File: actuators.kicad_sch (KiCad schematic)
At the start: 3 parts, among them J12 PWM signals, row 1, J13 SERVO_5V pass-through, row 2, J14 GND, row 3

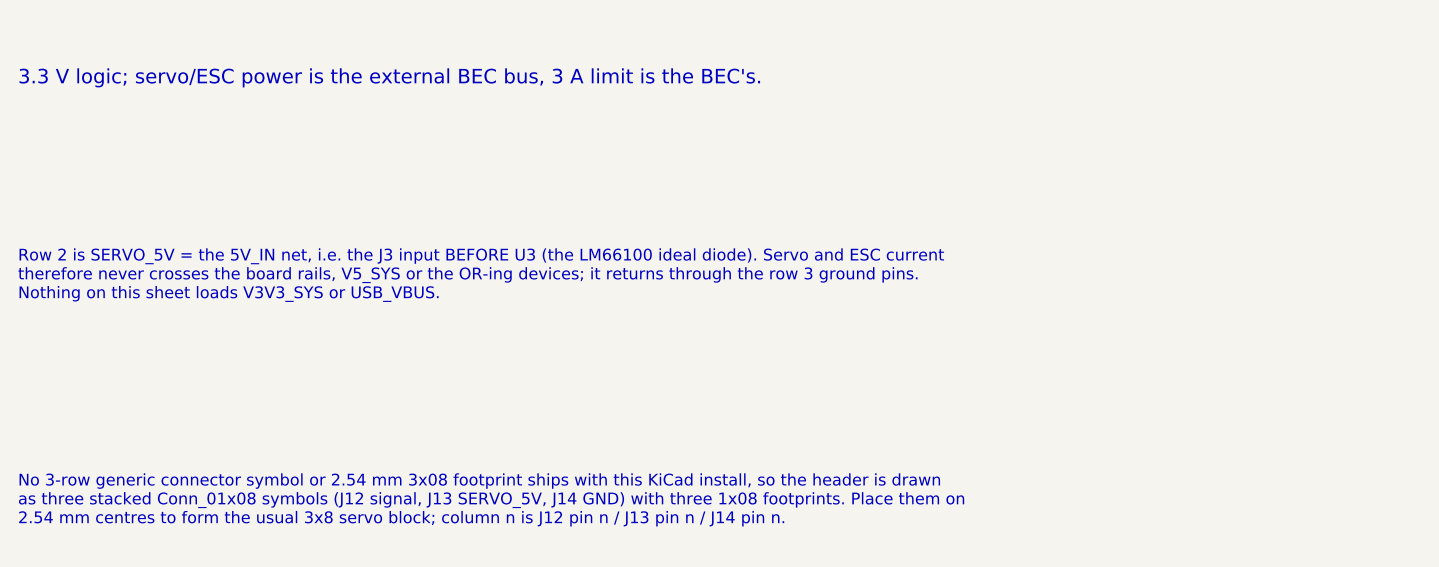
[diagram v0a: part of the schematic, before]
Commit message: Schematic review: TPS2121 input stage, DS-009 ports, sequencing and CS fixes; docs trimmed
Datasheet-grounded review of the full flight-controller schematic. Downstream
of the input everything verified pin-by-pin (TPS62913, TPS7A20, RP2354B,
BMI088/BMP581/ADXL375, W25Q128, microSD, PWM). The 5 V input stage did not:

- LM66100 (5.5 V rec-op / 6 V abs-max) replaced by one TPS2121 mux (U25):
  BEC priority on IN1, OV lockout ~5.86 V, current limit ~1.5 A, reverse
  blocking on both inputs, source status on GPIO39. Input spec 4.75-5.5 V.
- 5V_IN: 2x4.7 uF + 100 uF + SMAJ5.0A TVS; J3 JST-XH -> XT30PW-M (pin 1 GND).
- J6/J7/J9 reordered to Pixhawk DS-009 (VCC/sig/sig/GND); GPS/ELRS VCC 5 V.
- VIN_SENSE 22k/10k (full scale 10.6 V, was saturating at 5.5 V).
- TPS7A20 EN <- PWR_GOOD so V3V3_ANA rises after V3V3_SYS.
- RP2354B VREG_AVDD moved to V3V3_SYS (datasheet 6.1.8: must power up with
  VREG_VIN); ADC_AVDD stays on V3V3_ANA.
- 10k pull-ups on the four sensor chip-selects.
- ERC "global label appears once" re-enabled (0 hits).

Generator, netlist checker and SPICE decks updated (TPS2121 behavioral model,
new over-voltage and 2S mis-plug corners). Build idempotent, 143 pin mappings
PASS, ERC 0/0, all corners PASS.

Docs: POWER_*.md history removed, rationale folded into DESIGN_SPEC Decisions;
808 -> 290 lines across README, DESIGN_SPEC, LIBRARIES, simulations/README.

Co-Authored-By: Claude Fable 5.1 <noreply@anthropic.com>
Claude-Session: https://claude.ai/code/session_015cFNiWgf35VN2T43HaK8PE
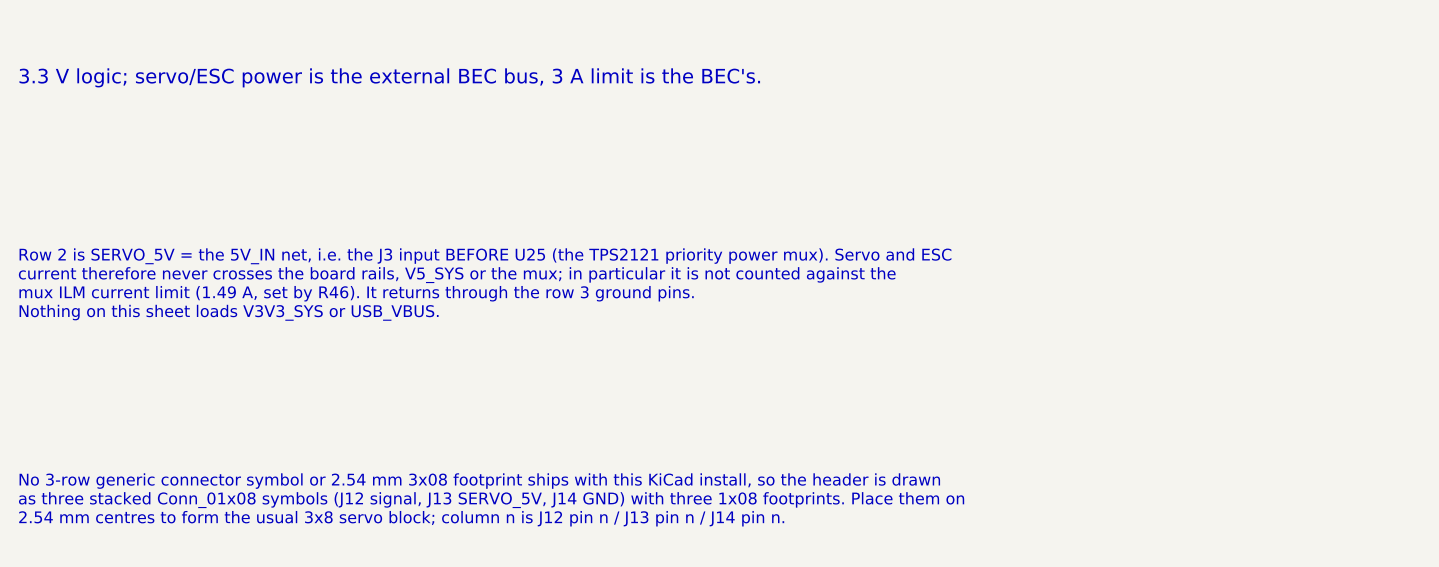
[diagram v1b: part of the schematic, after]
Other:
- note added: "Row 2 is SERVO_5V = the 5V_IN net, i.e. the J3 input BEFORE U25 (the TPS2121 priority power mux). Servo and ESC current therefore never crosses the board rails, V5_SYS or the mux; in particular it is not counted against the mux ILM current limit (1.49 A, set by R46). It returns through the row 3 ground pins. Nothing on this sheet loads V3V3_SYS or USB_VBUS."
- note removed: "Row 2 is SERVO_5V = the 5V_IN net, i.e. the J3 input BEFORE U3 (the LM66100 ideal diode). Servo and ESC current therefore never crosses the board rails, V5_SYS or the OR-ing devices; it returns through the row 3 ground pins. Nothing on this sheet loads V3V3_SYS or USB_VBUS."

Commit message: Physical design: VBAT-in buck, ESC pad row, pad-row IO, 50 mm single-sided board
Power: the FC now takes raw 2-6S VBAT from the MicoAir AM32 4-in-1 ESC pad
row (CURR TX M4 M3 M2 M1 VBAT GND, J3) through an AP63205WU 5 V/2 A buck
(U26, XGL4030-472, 3 x 22 uF) into the existing TPS2121 mux; XT30 and its
TVS removed. VBAT sense 100k/10k (36 V FS) on ADC0, ESC current sense on
ADC2, ESC KISS telemetry on GPIO30.

IO per the physical spec (DESIGN_SPEC "Physical design"): solder pad rows
for GPS/ELRS/MAG (JST-GH removed), DBG and buzzer; 3x4 servo block for
PWM5-8; 2x6 spare-IO block; WS2812C-2020 RGB LED replaces the two discrete
LEDs; buzzer moved off-board to pads; flash socket is the 150-mil SOIC-8
(W25Q64 default, APS6404L PSRAM alternative); four 4.0 mm grommet holes on
the 30.5 mm pattern. Passives moved to 0402/0603 for the single-sided
envelope.

Board: tools/setup_pcb.py regenerates MARV-V2.kicad_pcb from the netlist —
50 x 50 mm, 4-layer JLC 7628 stack-up, net classes incl. a 90 ohm USB pair,
edge-anchored connectors, coarse interior placement, silk pad labels.
DRC leaves only unrouted items. The BMP581 project footprint had its 2-pad
edges at +/-0.5 mm (corner pads overlapped, three nets shorted); corrected
to Bosch Fig. 32 (+/-0.25 mm, 0.20 mm gaps).

Checks: ERC 0/0, 217 pin mappings / 139 components, run_power_checks PASS,
audit 139/139, pcb DRC unrouted-only.

Co-Authored-By: Claude Fable 5.1 <noreply@anthropic.com>
Claude-Session: https://claude.ai/code/session_01U6Ud7JA3CDTJZVcZZr5sx1
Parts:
- J12: value PWM signals, row 1 -> PWM5-8 signals, row 1; footprint Connector_PinHeader_2.54mm:PinHeader_1x08_P2.54mm_Vertical -> MARV_Packages:PinHeader_1x04_P2.54mm_Vertical_ServoRow; symbol Connector_Generic:Conn_01x08 -> Connector_Generic:Conn_01x04
- J13: value SERVO_5V pass-through, row 2 -> Servo 5 V (5V_IN), row 2; footprint Connector_PinHeader_2.54mm:PinHeader_1x08_P2.54mm_Vertical -> MARV_Packages:PinHeader_1x04_P2.54mm_Vertical_ServoRow; symbol Connector_Generic:Conn_01x08 -> Connector_Generic:Conn_01x04
- J14: footprint Connector_PinHeader_2.54mm:PinHeader_1x08_P2.54mm_Vertical -> MARV_Packages:PinHeader_1x04_P2.54mm_Vertical_ServoRow; symbol Connector_Generic:Conn_01x08 -> Connector_Generic:Conn_01x04
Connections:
- net PWM1 is gone; now on net PWM5: J12.1 (Pin_1)
- net PWM2 is gone; now on net PWM6: J12.2 (Pin_2)
- net PWM3 is gone; now on net PWM7: J12.3 (Pin_3)
- net PWM4 is gone; now on net PWM8: J12.4 (Pin_4)
- net 5V_IN: no longer J13.5 (Pin_5), J13.6 (Pin_6), J13.7 (Pin_7), J13.8 (Pin_8)
- net GND: no longer J14.5 (Pin_5), J14.6 (Pin_6), J14.7 (Pin_7), J14.8 (Pin_8)
- net PWM5: no longer J12.5 (Pin_5)
- net PWM6: no longer J12.6 (Pin_6)
- net PWM7: no longer J12.7 (Pin_7)
- net PWM8: no longer J12.8 (Pin_8)
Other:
- note added: "PWM MAP (this sheet) PWM5 = GPIO10 PWM6 = GPIO11 PWM7 = GPIO14 PWM8 = GPIO15 ON THE ESC PAD ROW (J3, POWER 1) PWM1 = GPIO2 PWM2 = GPIO3 PWM3 = GPIO4 PWM4 = GPIO5"
- note added: "PWM5-8 only. PWM1-4 leave the board on the ESC pad row (J3, POWER 1) and appear nowhere on this sheet. Three 1x04 rows on 2.54 mm centres form the usual servo block: signal / 5 V / GND. No series resistors - 3.3 V logic straight from the RP2354B, which is what servos and ESCs expect."
- note added: "Row 2 is the 5V_IN net - the output of U26 (the AP63205 VBAT buck on POWER 1), taken BEFORE U25, the TPS2121 priority power mux. Servo current therefore never crosses V5_SYS or the mux and is not counted against the mux ILM current limit (1.49 A, set by R46); it does count against the buck, which is a 2 A part, so the four servo channels share whatever is left of 2 A after the avionics load (~0.3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"
- note added: "Three stacked Conn_01x04 symbols (J12 signal, J13 5 V, J14 GND) with three 1x04 THT footprints: no 3-row generic connector symbol or 2.54 mm 3x04 footprint ships with this KiCad install. Place them on 2.54 mm centres at the bottom-left of the board to form a 3x4 servo block in standard servo lead order (SIG / 5 V / GND); column n is J12 pin n / J13 pin n / J14 pin n. Through-hole 2.54 mm is delib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"
- note removed: "3.3 V logic; servo/ESC power is the external BEC bus, 3 A limit is the BEC's."
- note removed: "Eight PWM outputs on a 3-row 2.54 mm block: signal / SERVO_5V / GND. No series resistors - 3.3 V logic straight from the RP2354B, which is what servos and ESCs expect."
- note removed: "No 3-row generic connector symbol or 2.54 mm 3x08 footprint ships with this KiCad install, so the header is drawn as three stacked Conn_01x08 symbols (J12 signal, J13 SERVO_5V, J14 GND) with three 1x08 footprints. Place them on 2.54 mm centres to form the usual 3x8 servo block; column n is J12 pin n / J13 pin n / J14 pin n."
- note removed: "PWM MAP PWM1 = GPIO2 PWM5 = GPIO10 PWM2 = GPIO3 PWM6 = GPIO11 PWM3 = GPIO4 PWM7 = GPIO14 PWM4 = GPIO5 PWM8 = GPIO15"
- note removed: "Row 2 is SERVO_5V = the 5V_IN net, i.e. the J3 input BEFORE U25 (the TPS2121 priority power mux). Servo and ESC current therefore never crosses the board rails, V5_SYS or the mux; in particular it is not counted against the mux ILM current limit (1.49 A, set by R46). It returns through the row 3 ground pins. Nothing on this sheet loads V3V3_SYS or USB_VBUS."
- title: BOARD 4 / PWM outputs -> BOARD 4 / servo outputs PWM5-8
